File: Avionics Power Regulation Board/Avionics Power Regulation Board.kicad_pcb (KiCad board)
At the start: 2 copper layers, 62 parts, among them J1 Conn_01x06_Socket, J2 Conn_01x04_Socket, Q1 NMOS, Q2 NMOS, Q3 NMOS, SW1 SW_Push, U1 LM2576HVS-5, U2 BQ76920PW, U3 SC0917, U4 TPS61085DGK

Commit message: Updated Subscale Board
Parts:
- R3, R4: value 100Ohm -> 100
- moved U3 42.3 mm to (216.4, 74.9)
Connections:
- U3 pad 13: unconnected-(U3-GND-Pad13) -> GNDREF
- U3 pad 18: unconnected-(U3-GND-Pad18) -> GNDREF
- U3 pad 23: unconnected-(U3-GND-Pad23) -> GNDREF
- U3 pad 28: unconnected-(U3-GND-Pad28) -> GNDREF
- U3 pad 3: unconnected-(U3-GND-Pad3) -> GNDREF
- U3 pad 33: unconnected-(U3-AGND-Pad33) -> GNDREF
- U3 pad 38: unconnected-(U3-GND-Pad38) -> GNDREF
- U3 pad 39: unconnected-(U3-VSYS-Pad39) -> /VOUT
- U3 pad 8: unconnected-(U3-GND-Pad8) -> GNDREF
- U3 pad D2: unconnected-(U3-GND-PadD2) -> GNDREF

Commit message: Completely Redone
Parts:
- removed H3, H4, H5, H6: MountingHole, MountingHole:MountingHole_2.1mm
- removed J2: Conn_01x04_Socket, Connector_PinSocket_2.54mm:PinSocket_1x04_P2.54mm_Vertical
- removed U3: SC0917, SC0917:MODULE_SC0917
- added G***: LOGO, AIAA Logo:AIAA Logo, B.Cu at (124.0, 95.9)
- C2: footprint Capacitor_THT:C_Radial_D5.0mm_H11.0mm_P2.00mm -> Capacitor_THT:C_Radial_D10.0mm_H16.0mm_P5.00mm
- J1: value Conn_01x06_Socket -> Conn_01x05_Socket; footprint Connector_PinSocket_2.54mm:PinSocket_1x06_P2.54mm_Vertical -> Connector_PinHeader_2.54mm:PinHeader_1x05_P2.54mm_Vertical
- L1: footprint RLB9012-101KL:IND_RLB9012-101KL -> Inductor_THT:L_Radial_D6.0mm_P4.00mm
- R1, R2, R3, R4, R5, R6, R7, R8, R9, RC1, RC2, RC3, RC4, RC5, RF1, RSNS1, Rcomp1: footprint MFR_25FRF52_10K:RESAD1100W55L680D260 -> Resistor_SMD:R_0805_2012Metric_Pad1.20x1.40mm_HandSolder
- moved H1 147.6 mm to (207.0, 140.8)
- moved H2 115.2 mm to (207.0, 57.2)
- moved J1 108.2 mm to (170.2, 58.4), turned to 90 degrees
- moved RF1 107.9 mm to (168.9, 71.1), turned to 180 degrees
- moved Ccomp1 106.4 mm to (177.5, 101.0)
- moved RSNS1 106.4 mm to (203.7, 64.8), turned to -90 degrees
- moved D2 104.8 mm to (170.5, 123.0)
- moved RC5 104.7 mm to (184.9, 63.1), turned to 180 degrees
- moved D6 100.3 mm to (207.4, 77.5), turned to 90 degrees
- moved RC4 97.0 mm to (185.1, 67.1), turned to 180 degrees
- moved R2 96.0 mm to (168.8, 104.8), turned to 180 degrees
- moved R1 94.9 mm to (168.8, 107.1)
- moved Rcomp1 93.3 mm to (173.5, 101.8)
- moved RC3 89.4 mm to (185.1, 71.2), turned to 180 degrees
- moved D3 88.7 mm to (193.6, 68.6)
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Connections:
- J1 pad 1: unconnected-(J1-Pin_1-Pad1) -> GNDREF
- J1 pad 2: unconnected-(J1-Pin_2-Pad2) -> /VOUT
- J1 pad 3: unconnected-(J1-Pin_3-Pad3) -> /SDA
- J1 pad 4: unconnected-(J1-Pin_4-Pad4) -> /SCL
- J1 pad 5: unconnected-(J1-Pin_5-Pad5) -> /ALERT
- U2 pad 20: /Battery Monitor System/ALERT -> /ALERT
- U2 pad 4: /Battery Monitor System/SDA -> /SDA
- U2 pad 5: /Battery Monitor System/SCL -> /SCL
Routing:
- net Net-(BT1-Pad1+): track 0.00 -> 150.6 mm, vias 0 -> 2
- net Net-(BT1-Pad2+): track 0.00 -> 134.1 mm, vias 0 -> 2
- net Net-(BT1-Pad3+): track 0.00 -> 128.6 mm
- net GNDREF: track 0.00 -> 84.4 mm, vias 0 -> 4
- net /REGOUT: track 0.00 -> 78.5 mm, vias 0 -> 2
- net /VIN: track 0.00 -> 62.1 mm, vias 0 -> 1
- net /Battery Monitor System/SRN: track 0.00 -> 54.3 mm, vias 0 -> 4
- net /Battery Monitor System/BAT +: track 0.00 -> 54.1 mm
- net /Battery Monitor System/VC1: track 0.00 -> 52.6 mm, vias 0 -> 1
- net /Battery Monitor System/SRP: track 0.00 -> 51.4 mm, vias 0 -> 1
- net /Battery Monitor System/VC5: track 0.00 -> 44.1 mm, vias 0 -> 1
- net Net-(D3-K): track 0.00 -> 43.7 mm, vias 0 -> 2
- net /Battery Monitor System/VC3: track 0.00 -> 39.3 mm, vias 0 -> 1
- net /Battery Monitor System/CHG: track 0.00 -> 34.3 mm, vias 0 -> 2
- net /Battery Monitor System/VC2: track 0.00 -> 33.8 mm, vias 0 -> 1
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- added copper zone on F.Cu, net /VOUT
- added copper zone on B.Cu, net GNDREF
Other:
- board outline added: 125.4 x 88.8 mm

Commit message: Small Edits
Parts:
- moved H1 8.25 mm to (207.1, 132.6)
- moved U1 7.29 mm to (195.7, 127.9)
- moved L1 7.22 mm to (189.1, 114.0)
- moved C1 2.12 mm to (181.6, 119.1)
- moved H2 0.08 mm to (207.1, 57.2)
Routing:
- net Net-(D1-K): track 28.3 -> 24.6 mm
- net GNDREF: track 84.4 -> 87.0 mm
- net /VOUT: track 4.90 -> 6.77 mm
- net /VIN: track 62.1 -> 61.2 mm
- net /Battery Monitor System/DSG: track 30.9 -> 30.3 mm, vias 1 -> 0
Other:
- board size 125.4 x 88.8 mm -> 127.4 x 80.5 mm
- board text added: "+"

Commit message: Miku
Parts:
- added G***: LOGO, Miku:Miku, F.Cu at (123.8, 95.7)

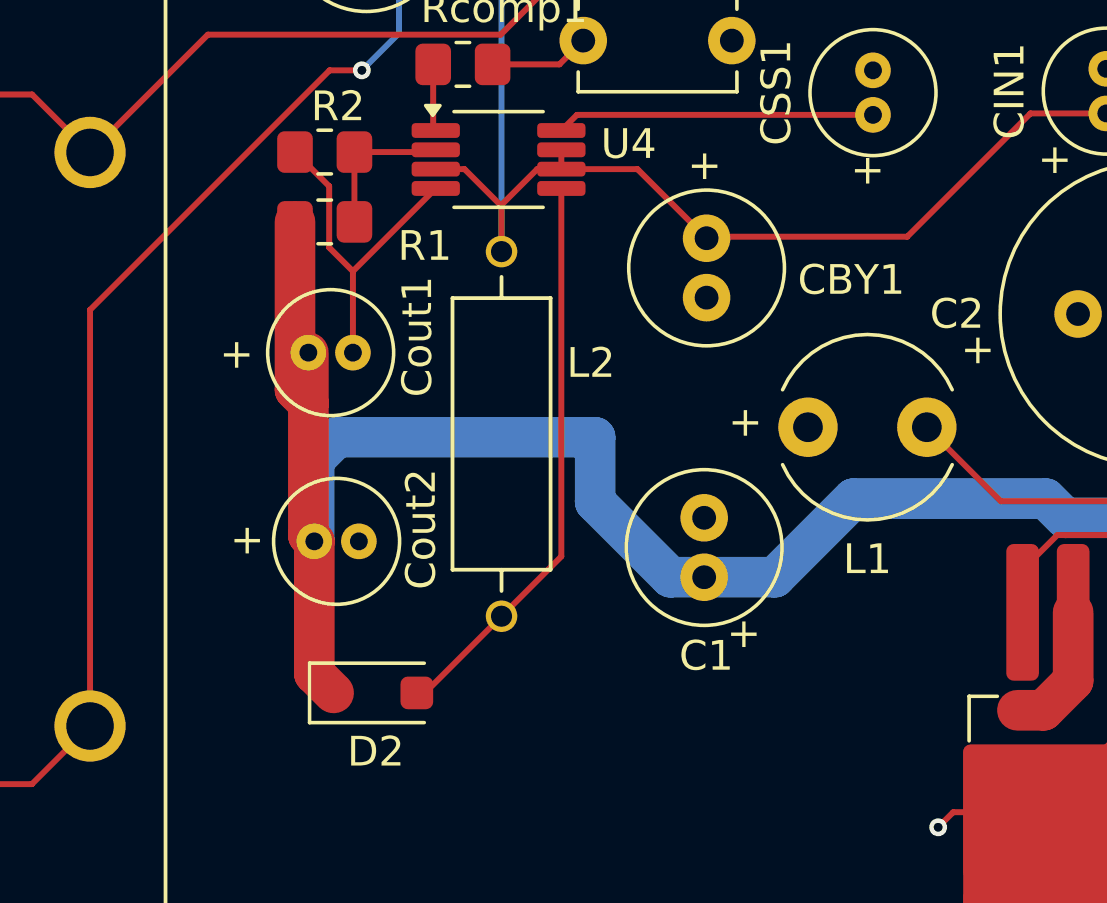
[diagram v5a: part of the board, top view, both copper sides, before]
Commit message: Changed Inductor
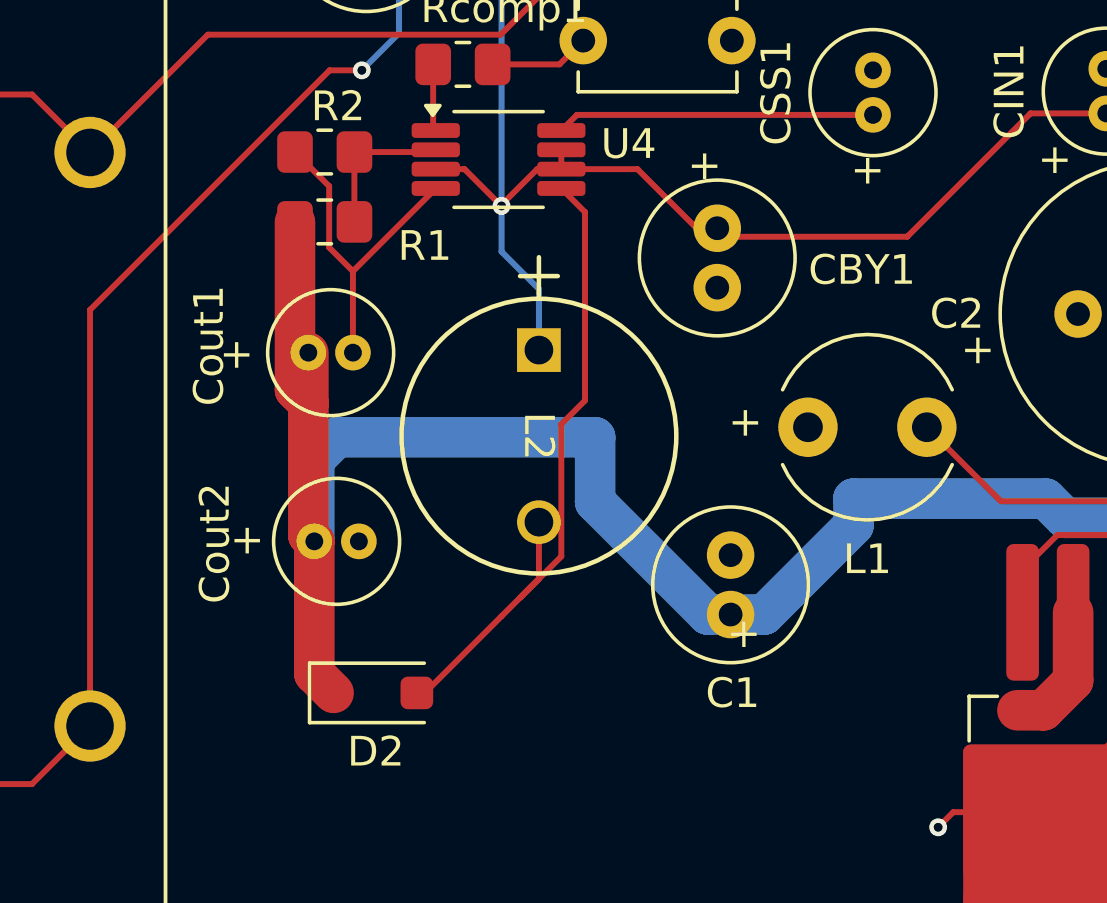
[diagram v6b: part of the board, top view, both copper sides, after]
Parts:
- L2: footprint AIAP-01-3R3K-T:INDAD1227W51L914D355 -> 3.3uH:IND_BOURNS_RLB9012
- moved L2 3.09 mm to (176.1, 111.5)
- moved C1 1.54 mm to (182.5, 120.3)
- moved CBY1 0.49 mm to (182.1, 107.3)
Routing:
- net Net-(D2-A): track 19.1 -> 22.6 mm
- net /REGOUT: track 78.5 -> 80.8 mm, vias 2 -> 3
- net /VIN: track 61.2 -> 62.7 mm

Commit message: Small Changes
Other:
- board text added: "1 GND 2 VCC"
- board text added: "3 SDA 4 SCL"
- board text added: "5 ALERT"
- board text added: "J1 Pins"
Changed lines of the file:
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@@
 		)
+	)
+	(gr_rect
+		(start 168.25 126.7)
+		(end 185.8 132.25)
+		(stroke
+			(width 0.1)
+			(type default)
+		)
+		(fill none)
+		(layer "F.SilkS")
 	)
 	(gr_line
@@
 		)
 	)
+	(gr_text "1 GND\n2 VCC"
+		(at 168.65 130.9 0)
+		(layer "F.SilkS")
+		(effects
+			(font
+				(size 1 1)
+				(thickness 0.1)
+			)
+			(justify left bottom)
+		)
+	)
 	(gr_text "+"
 		(at 181.0512 105.8164 0)
@@
 			)
 			(justify left bottom)
+		)
+	)
+	(gr_text "3 SDA\n4 SCL\n"
+		(at 173.95 130.95 0)
+		(layer "F.SilkS")
+		(effects
+			(font
+				(size 1 1)
+				(thickness 0.1)
+			)
+			(justify left bottom)
+		)
+	)
+	(gr_text "5 ALERT"
+		(at 178.8 130.1 0)
+		(layer "F.SilkS")
+		(effects
+			(font
+				(size 1 1)
+				(thickness 0.1)
+			)
+			(justify left bottom)
+		)
+	)
+	(gr_text "J1 Pins\n\n"
+		(at 173.75 127.95 0)
+		(layer "F.SilkS")
+		(effects
+			(font
+				(size 1 1)
+				(thickness 0.1)
+			)
+			(justify left bottom)

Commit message: Small Updates
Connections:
- D6 pad 2: Net-(D6-A) -> GNDREF
- Q3 pad 3: Net-(D6-A) -> GNDREF
- R8 pad 1: Net-(D6-A) -> GNDREF
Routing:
- net Net-(D6-A): track 27.6 -> 0.00 mm
- net GNDREF: track 87.0 -> 98.4 mm
